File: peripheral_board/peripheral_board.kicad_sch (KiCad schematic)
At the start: 131 parts, among them CN1 DF11-16DP-2DSA(08), J1 Conn_01x06, J2 Conn_ARM_JTAG_SWD_10, J3 Conn_01x03, J4 Conn_01x03, J5 Conn_01x05, SW1 EVPAA602W, SW2 EVPAA602W, SW3 EVPAA602W, U1 RP2040, U2 W5500, U3 AZ1117CH-3.3TRG1, U4 SN74AHC1G125DBVR, U5 KSZ8795CLXIC, U6 W25Q128JVSIQTR, Y1 12MHZ, Y2 25MHZ, Y3 25MHZ

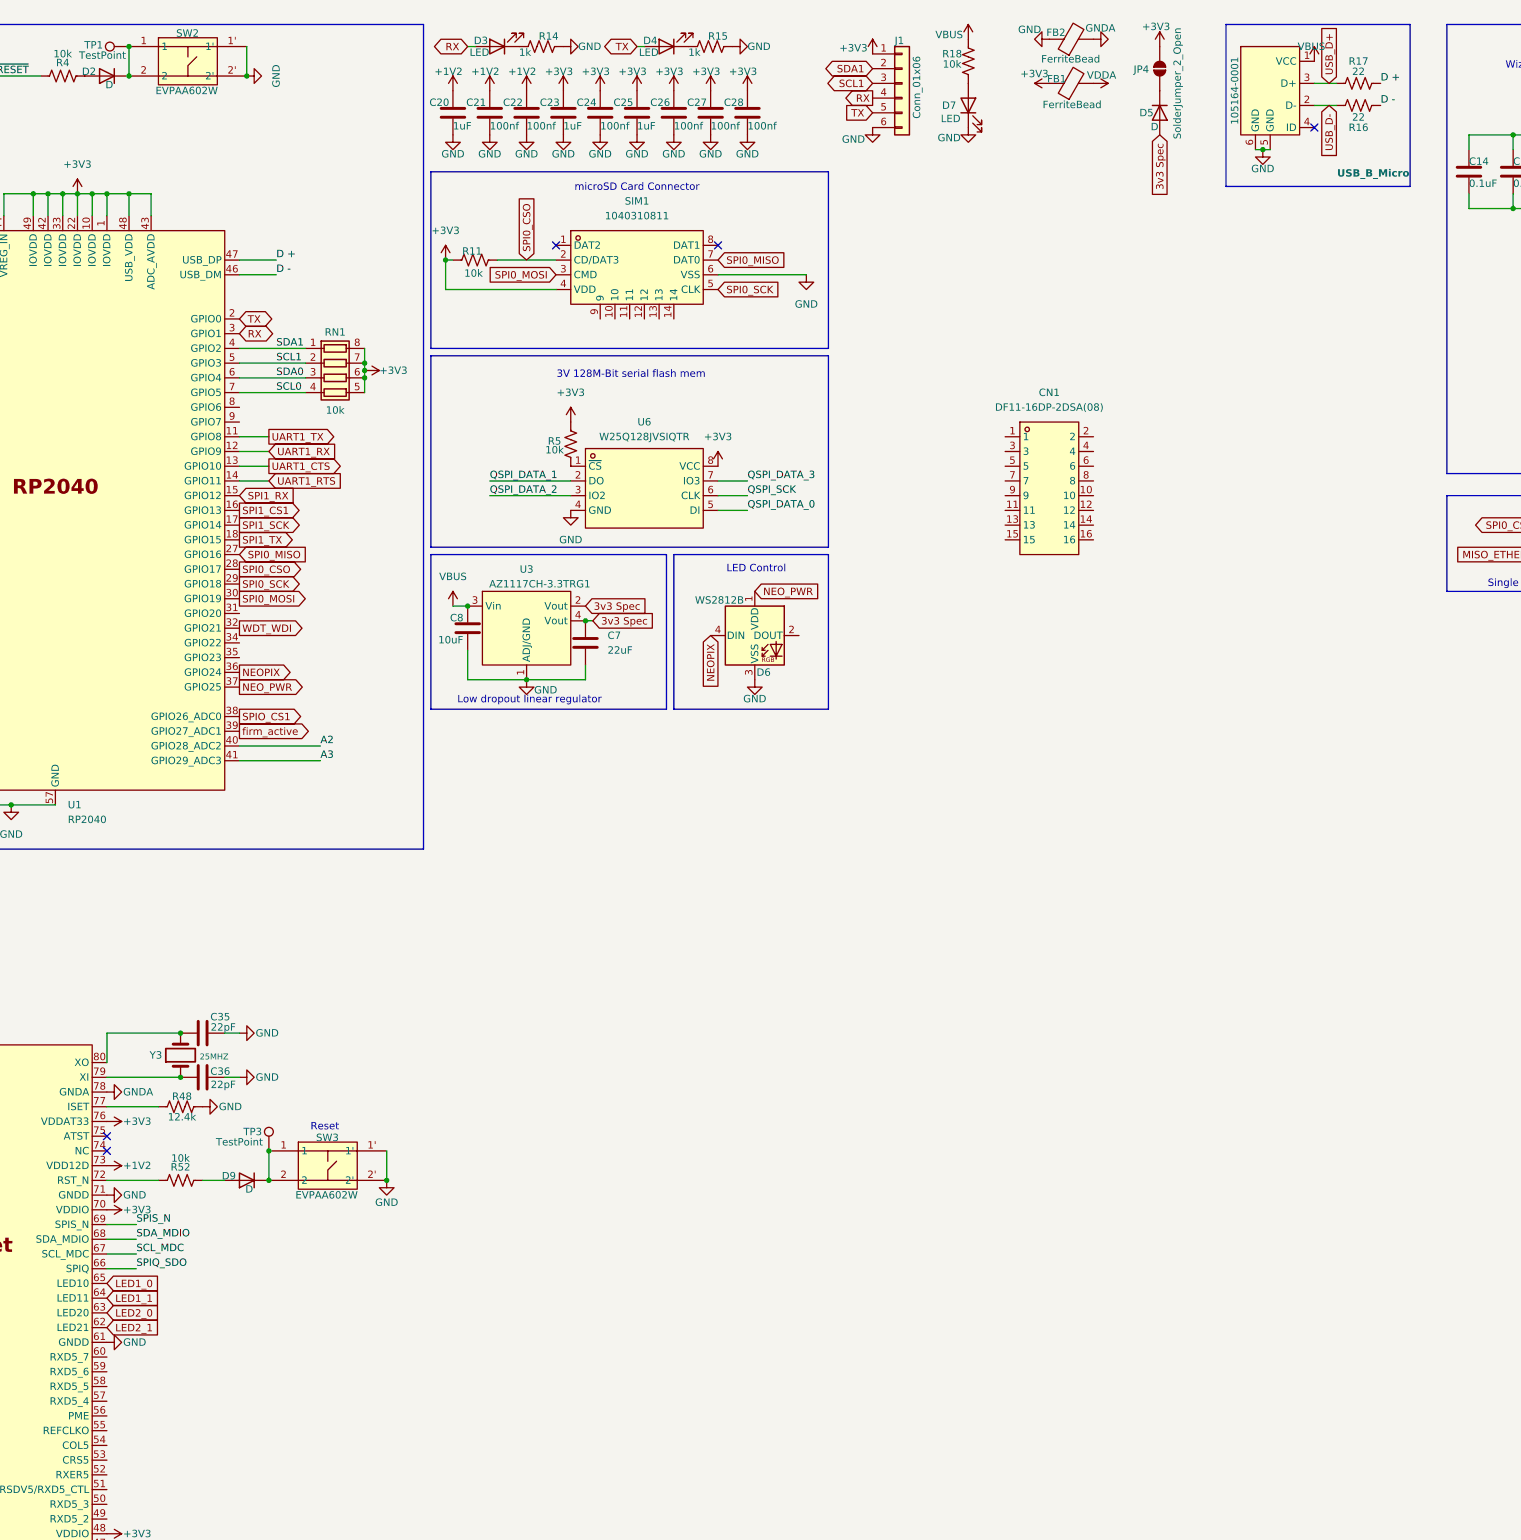
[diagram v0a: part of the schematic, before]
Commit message: Added some labels to the WIP
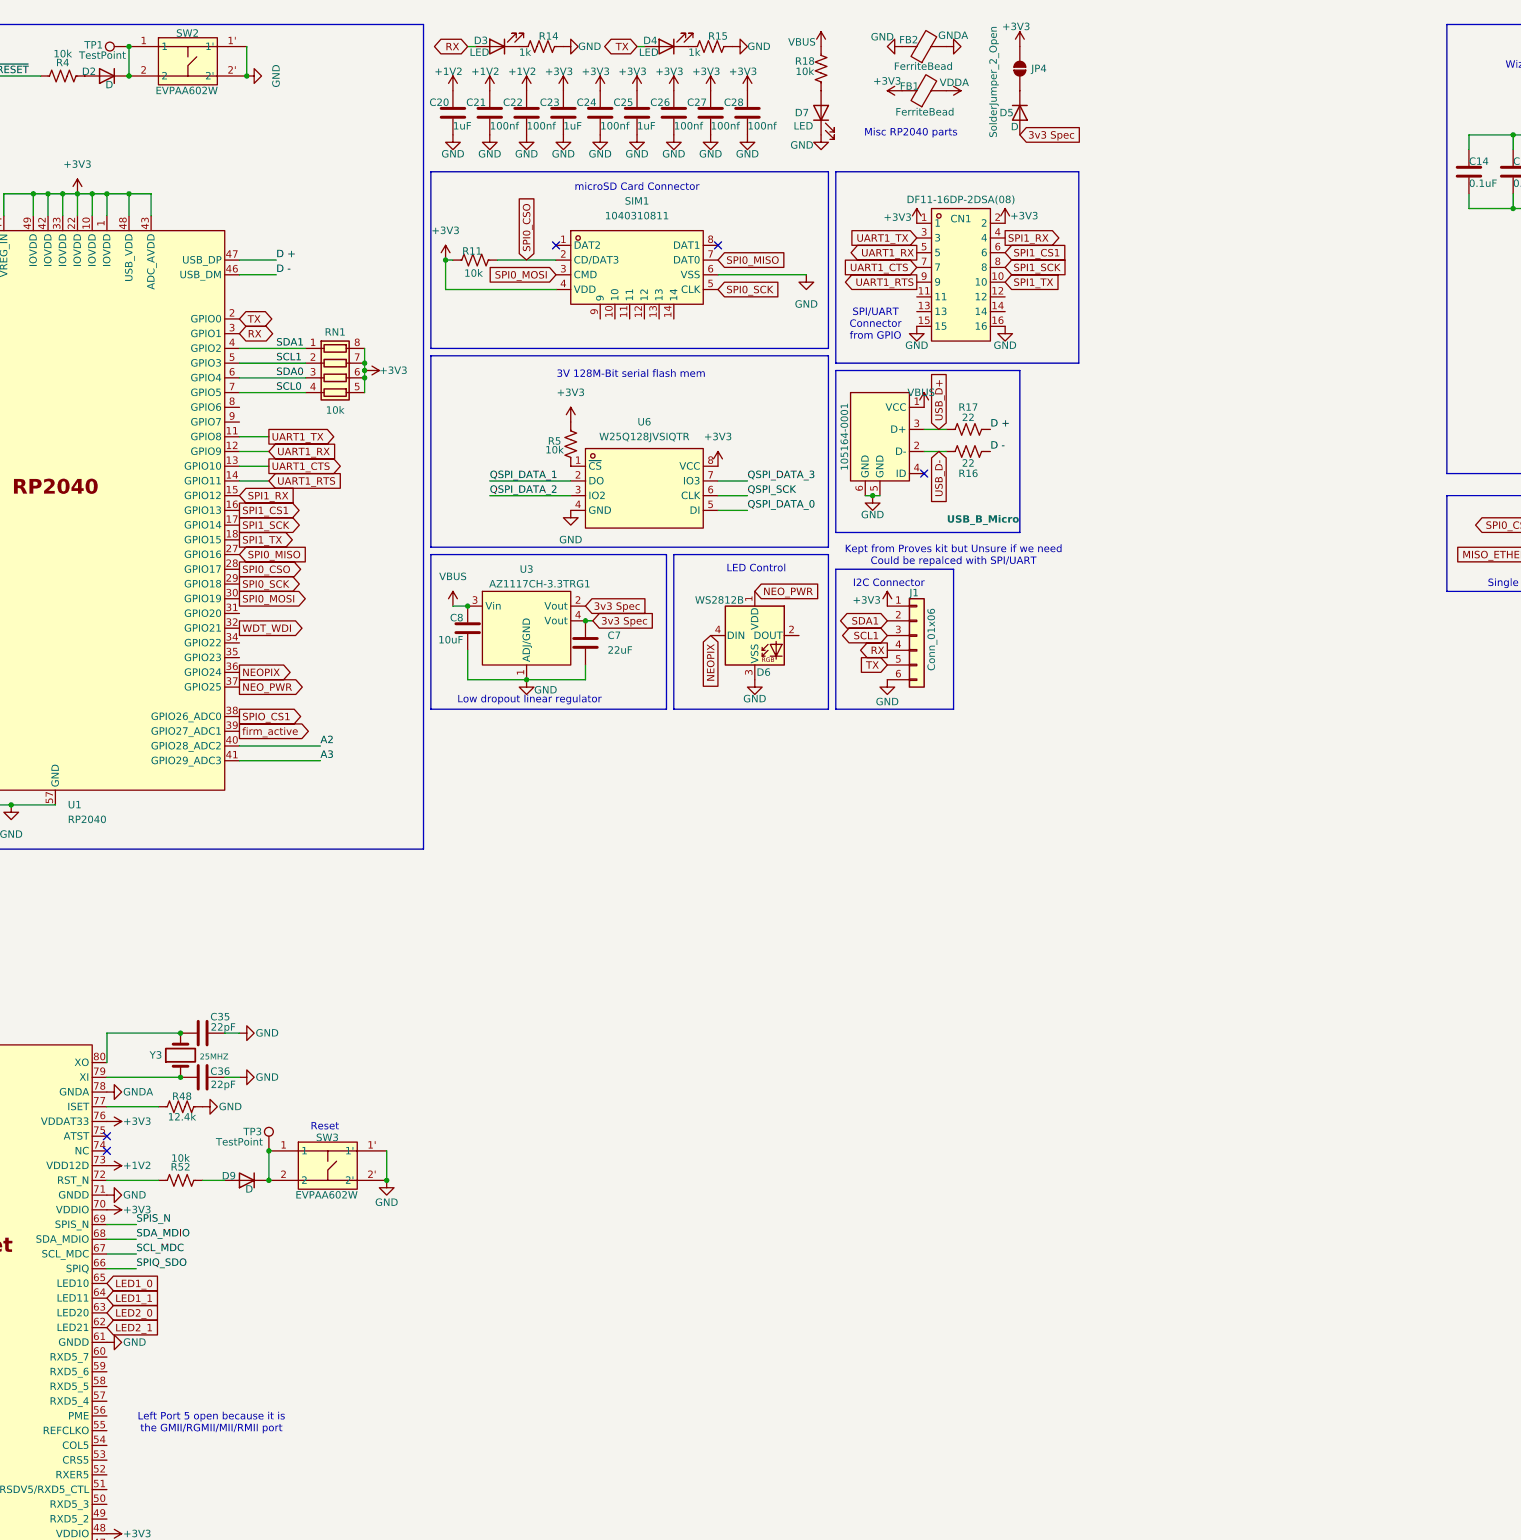
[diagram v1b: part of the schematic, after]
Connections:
- net +3V3: now also CN1.1, CN1.2
- net GND: now also CN1.15, CN1.16
- net SPI1_CS1: now also CN1.6
- net SPI1_RX: now also CN1.4
- net SPI1_SCK: now also CN1.8
- net SPI1_TX: now also CN1.10
- net UART1_CTS: now also CN1.7
- net UART1_RTS: now also CN1.9
- net UART1_RX: now also CN1.5
- net UART1_TX: now also CN1.3
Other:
- note added: "I2C Connector"
- note added: "Kept from Proves kit but Unsure if we need Could be repalced with SPI/UART"
- note added: "Left Port 5 open because it is the GMII/RGMII/MII/RMII port"
- note added: "Misc RP2040 parts"
- note added: "SPI/UART Connector from GPIO"
- moved on the sheet: CN1, D5, D7, FB1, FB2, J1, JP4, R16, R17, R18, USB_B_Micro

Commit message: Add a few changes with some labels
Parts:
- added D10, D11: LED, LED_SMD:LED_0603_1608Metric, symbol Device:LED
- added R53, R55: 330, Resistor_SMD:R_0603_1608Metric, symbol Device:R_US
- added R54, R56: 4.7k, Resistor_SMD:R_0603_1608Metric, symbol Device:R_US
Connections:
- net +3V3: now also R53.2, R54.1, R55.2, R56.1
- net INTR_N: now reaches U5.23 (INTR_N)
- net INTR_N: now also D10.1 (K), R54.2
- net PME_N: now reaches U5.56 (PME)
- net PME_N: now also D11.1 (K), R56.2
- new net: D11.2 (A), R55.1
- new net: D10.2 (A), R53.1
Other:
- note added: "Can remove the 100nf caps"
- note added: "INT"
- note added: "PME"
- company: (none) -> Bronco Space
- title: (none) -> Peripheral Board with Ethernet Switch
- moved on the sheet: C35, C36, D9, R48, R52, SW3, TP3, U4, U5, Y3

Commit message: Added libraries
Added some global libraries to local for ease of use. Added decoupling caps from the dev board.
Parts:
- added C33, C37, C40, C42, C45, C47, C48, C49: 0.1uF, Capacitor_SMD:C_0402_1005Metric, symbol Device:C
- added C34, C39, C41: 100uF, Capacitor_SMD:C_0402_1005Metric, symbol Device:C
- added C38, C43: 0.01uF, Capacitor_SMD:C_0402_1005Metric, symbol Device:C
- added C44, C46: 22uF, Capacitor_SMD:C_0402_1005Metric, symbol Device:C
- added FB3, FB4: FerriteBead, Inductor_SMD:L_0603_1608Metric, symbol Device:FerriteBead
- added JP5, JP6: SolderJumper_2_Open, Jumper:SolderJumper-2_P1.3mm_Open_RoundedPad1.0x1.5mm, symbol Jumper:SolderJumper_2_Open
- added U7: NCP130AMX120TCG, easyeda2kicad:XDFN-6_L1.2-W1.2-P0.40-BL-EP, symbol easyeda2kicad_local:NCP130AMX120TCG
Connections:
- net GND: now also FB2.2, C33.1, C34.1, C37.1, C38.1, C39.1, C40.1, C41.1, C42.1, C43.1, C44.1, C45.1, C46.1, C47.1, C48.1, C49.1, U7.5 (GND), U7.7 (EP); no longer FB2.1
- net GNDA: now also FB2.1; no longer FB2.2
- new net: FB3.2, JP5.2 (B)
- new net: C39.2, C40.2, FB3.1, FB4.1, U7.1 (VOUT)
- new net: FB4.2, JP6.2 (B)
- new net +5V: C33.2, U7.3 (EN), U7.4 (BIAS), U7.6 (VIN)
- new net V1.2A: C34.2, C37.2, C38.2, C44.2, C45.2, JP5.1 (A)
- new net V1.2D: C41.2, C42.2, C43.2, C46.2, C47.2, C48.2, C49.2, JP6.1 (A)
- no-connect marks 22 -> 23
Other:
- note added: "1.2V Digital Current Probe"
- note added: "Decoupling Device Pin 1 VDD12A for analog 1.2V"
- note added: "Decoupling Device Pin 26, 42 & 73 for VDD12D for digital 1.2V"
- note added: "Page 5 of the Ethernet switch data sheet"
- note added: "V1.2A Current Probe"
- moved on the sheet: C35, C36, D10, D11, D9, J3, J4, J5, R48, R49, R50, R51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

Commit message: Slight update
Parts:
- JP1, JP2, JP3, JP4, JP5, JP6: now in the parts list
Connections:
- net SPIO_CS1 is gone; now on net SPI0_CS1: U1.38 (GPIO26_ADC0)
- net +1V2: no longer U5.1 (VDD12A), U5.26 (VDD12D), U5.42 (VDD12D), U5.73 (VDD12D)
- net V1.2A: now also U5.1 (VDD12A)
- net V1.2D: now also U5.26 (VDD12D), U5.42 (VDD12D), U5.73 (VDD12D)
- net A2: no longer names the net of U1.40 (GPIO28_ADC2)
- net A3: no longer names the net of U1.41 (GPIO29_ADC3)
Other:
- note added: "Can remove the 100nf caps According to Andrew"
- note added: "Should this be coupled with ~{RESET}"
- note removed: "Can remove the 100nf caps"
- moved on the sheet: D9, R52, SW3, TP3

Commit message: Created subpages
Added subpages for the schematic
Did a quick overview
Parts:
- removed C1, C19, C2, C3, C35, C36, C4, C5, C9: 22pF, Capacitor_SMD:C_0402_1005Metric, symbol Device:C
- removed C10, C15, C18, C8: 10uF, Capacitor_SMD:C_0402_1005Metric, symbol Device:C
- removed C11, C12, C13, C14, C16, C17, C33, C37, C40, C42, C45, C47, C48, C49: 0.1uF, Capacitor_SMD:C_0402_1005Metric, symbol Device:C
- removed C20, C23, C25: 1uF, Capacitor_SMD:C_0402_1005Metric, symbol Device:C
- removed C21, C22, C24, C26, C27, C28: 100nf, Capacitor_SMD:C_0402_1005Metric, symbol Device:C
- removed C29, C30, C31, C32: 1000pf, Capacitor_SMD:C_0402_1005Metric, symbol Device:C
- removed C34, C39, C41: 100uF, Capacitor_SMD:C_0402_1005Metric, symbol Device:C
- removed C38, C43: 0.01uF, Capacitor_SMD:C_0402_1005Metric, symbol Device:C
- removed C44, C46, C7: 22uF, Capacitor_SMD:C_0402_1005Metric, symbol Device:C
- removed C6: 10nf, Capacitor_SMD:C_0402_1005Metric, symbol Device:C
- removed CN1: DF11-16DP-2DSA(08), easyeda2kicad:CONN-TH_DF11-16DP-2DSA-08, symbol easyeda2kicad:DF11-16DP-2DSA(08)
- removed D1, D2, D5, D9: D, Diode_SMD:D_SOD-323F, symbol Device:D
- removed D10, D11, D3, D4, D7, D8: LED, LED_SMD:LED_0603_1608Metric, symbol Device:LED
- removed D6: WS2812B, LED_SMD:LED_WS2812B_PLCC4_5.0x5.0mm_P3.2mm, symbol LED:WS2812B
- removed FB1, FB2, FB3, FB4: FerriteBead, Inductor_SMD:L_0603_1608Metric, symbol Device:FerriteBead
- removed J1: Conn_01x06, Connector_PinHeader_2.54mm:PinHeader_1x06_P2.54mm_Vertical, symbol Connector_Generic:Conn_01x06
- removed J2: Conn_ARM_JTAG_SWD_10, symbol Connector:Conn_ARM_JTAG_SWD_10
- removed J3, J4: Conn_01x03, Connector_Molex:Molex_KK-396_A-41791-0003_1x03_P3.96mm_Vertical, symbol Connector_Generic:Conn_01x03
- removed J5: Conn_01x05, Connector_PinHeader_1.00mm:PinHeader_1x05_P1.00mm_Vertical, symbol Connector_Generic:Conn_01x05
- removed JP1, JP2, JP3, JP4, JP5, JP6: SolderJumper_2_Open, Jumper:SolderJumper-2_P1.3mm_Open_RoundedPad1.0x1.5mm, symbol Jumper:SolderJumper_2_Open
- removed R1, R11, R18, R19, R2, R3, R4, R49, R5, R50, R51, R52: 10k, Resistor_SMD:R_0603_1608Metric, symbol Device:R_US
- removed R10, R6, R7, R8: 49.9, Resistor_SMD:R_0603_1608Metric, symbol Device:R_US
- removed R12: 1M, Resistor_SMD:R_0603_1608Metric, symbol Device:R_US
- removed R13, R48: 12.4k, Resistor_SMD:R_0603_1608Metric, symbol Device:R_US
- removed R14, R15: 1k, Resistor_SMD:R_0603_1608Metric, symbol Device:R_US
- removed R16, R17: 22, Resistor_SMD:R_0603_1608Metric, symbol Device:R_US
- removed R20, R21, R22, R23, R24, R25, R27, R28, R29, R30, R31, R32, R34, R35, R36, R37, R38, R39, R40, R41, R42, R43, R44, R45: 51, Resistor_SMD:R_0603_1608Metric, symbol Device:R_US
- removed R26, R33, R46, R47: 75, Resistor_SMD:R_0603_1608Metric, symbol Device:R_US
- removed R53, R55: 330, Resistor_SMD:R_0603_1608Metric, symbol Device:R_US
- removed R54, R56: 4.7k, Resistor_SMD:R_0603_1608Metric, symbol Device:R_US
- removed R9: 10, Resistor_SMD:R_0603_1608Metric, symbol Device:R_US
- removed RJ2, RJ3, RJ4, RJ5, RJ6: RJHSE5384, easyeda2kicad:RJ45-TH_RJHSE5384, symbol easyeda2kicad:RJHSE5384
- removed RN1, RN2: 10k, Resistor_SMD:R_Array_Convex_4x0603, symbol Device:R_Pack04
- removed SIM1: 1040310811, easyeda2kicad:SIM-SMD_8P-1040310811, symbol easyeda2kicad:1040310811
- removed SW1, SW2, SW3: EVPAA602W, easyeda2kicad:KEY-TH_4P-L3.5-W4.9-P2.80-LS4.3, symbol easyeda2kicad:EVPAA602W
- removed TP1, TP2, TP3: TestPoint, symbol Connector:TestPoint
- removed U1: RP2040, easyeda2kicad:LQFN-56_L7.0-W7.0-P0.4-EP, symbol easyeda2kicad:RP2040
- removed U2: W5500, easyeda2kicad:LQFP-48_L7.0-W7.0-P0.50-LS9.0-BL, symbol easyeda2kicad:W5500
- removed U3: AZ1117CH-3.3TRG1, easyeda2kicad:SOT-223-3_L6.5-W3.4-P2.30-LS7.0-BR, symbol easyeda2kicad:AZ1117CH-3.3TRG1
- removed U4: SN74AHC1G125DBVR, easyeda2kicad:SOT-23-5_L3.0-W1.7-P0.95-LS2.8-BR, symbol easyeda2kicad:SN74AHC1G125DBVR
- removed U5: KSZ8795CLXIC, easyeda2kicad:LQFP-80_L10.0-W10.0-P0.40-LS12.2-BL, symbol easyeda2kicad:KSZ8795CLXIC
- removed U6: W25Q128JVSIQTR, easyeda2kicad:SOIC-8_L5.3-W5.3-P1.27-LS8.0-BL, symbol easyeda2kicad:W25Q128JVSIQTR
- removed U7: NCP130AMX120TCG, easyeda2kicad:XDFN-6_L1.2-W1.2-P0.40-BL-EP, symbol easyeda2kicad_local:NCP130AMX120TCG
- removed USB_B_Micro: 105164-0001, easyeda2kicad:MICRO-USB-SMD_5P-P0.65-H-F_105164-0001, symbol easyeda2kicad:105164-0001
- removed Y1: 12MHZ, Crystal:Crystal_SMD_2012-2Pin_2.0x1.2mm, symbol Device:Crystal
- removed Y2: 25MHZ, Crystal:Crystal_SMD_3225-4Pin_3.2x2.5mm, symbol Device:Crystal
- removed Y3: 25MHZ, Crystal:Crystal_SMD_2012-2Pin_2.0x1.2mm, symbol Device:Crystal
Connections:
- no-connect marks 23 -> 0
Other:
- added sheet 5-Port_Ethernet_Switch (ethernet_switch.kicad_sch)
- added sheet Raspberry_pi (rp.kicad_sch)
- added sheet Wiznet (Wiznet.kicad_sch)
- note removed: "0 0 0 = 10BT Half-duplex, Auto-negotiation disabled 0 0 1 = 10BT Full-duplex, Auto-negotiation disabled 0 1 0 = 100BT Half-duplex, Auto-negotiation disabled 0 1 1 = 100BT Full-duplex, Auto-negotiation disabled 1 0 0 = 100BT Half-duplex, Auto-negotiation enabled 1 1 1 = All capable, Auto-negotiation enabled (DEFAULT)"
- note removed: "1.2V Digital Current Probe"
- note removed: "3V 128M-Bit serial flash mem"
- note removed: "Arm 10-pin, 0.05" JTAG/SWD connector"
- note removed: "Breakout Pins"
- note removed: "Can remove the 100nf caps According to Andrew"
- note removed: "Decoupling Device Pin 1 VDD12A for analog 1.2V"
- note removed: "Decoupling Device Pin 26, 42 & 73 for VDD12D for digital 1.2V"
- note removed: "Green(9) is Speed WHICH IS LED#_1 Yellow(11) is Link/Act WHICH IS LED#_0"
- note removed: "I2C Connector"
- note removed: "INT"
- note removed: "Kept from Proves kit but Unsure if we need Could be repalced with SPI/UART"
- note removed: "LED Control"
- note removed: "Left Port 5 open because it is the GMII/RGMII/MII/RMII port"
- note removed: "Low dropout linear regulator"
- note removed: "Misc RP2040 parts"
- note removed: "PME"
- note removed: "Page 5 of the Ethernet switch data sheet"
- note removed: "RJ45 Port 1"
- note removed: "RJ45 Port 2"
- note removed: "RJ45 Port 3"
- note removed: "RJ45 Port 4"
- note removed: "RJ45 connector"
- note removed: "Reset"
- note removed: "SPI/UART Connector from GPIO"
- note removed: "Should this be coupled with ~{RESET}"
- note removed: "Single Bus Buffer gate with 3-state output"
- note removed: "V1.2A Current Probe"
- note removed: "Wiznet Ethernet controller"
- note removed: "microSD Card Connector"

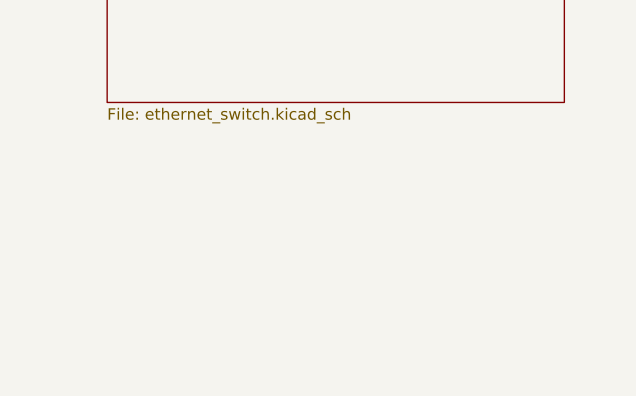
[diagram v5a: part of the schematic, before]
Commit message: Put in the strap in mode
Found a different configuration that should work as the 4 port switch. Added the courtyards to all the parts.
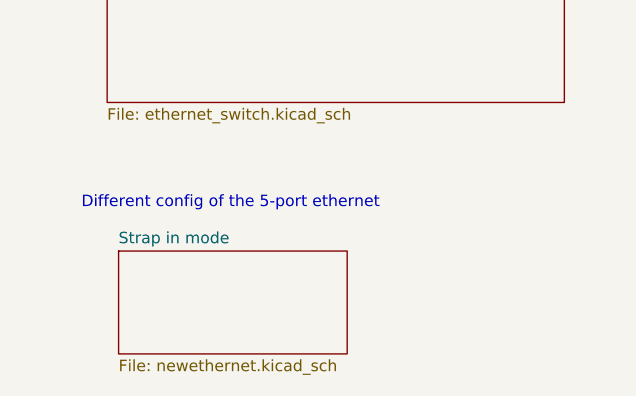
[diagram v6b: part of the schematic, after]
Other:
- added sheet Strap in mode (newethernet.kicad_sch)
- note added: "Different config of the 5-port ethernet"
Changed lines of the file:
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@@
 		(comment 2 "By John Pollak")
+	)
+	(text "Different config of the 5-port ethernet\n"
+		(exclude_from_sim no)
+		(at 39.116 125.476 0)
+		(effects
+			(font
+				(size 1.27 1.27)
+			)
+		)
 	)
 	(sheet
@@
 				)
 			)
+		)
+	)
+	(sheet
+		(at 26.67 130.81)
+		(size 25.4 11.43)
+		(exclude_from_sim yes)
+		(in_bom no)
+		(on_board no)
+		(dnp yes)
+		(fields_autoplaced yes)
+		(stroke
+			(width 0.1524)
+			(type solid)
+		)
+		(fill
+			(color 0 0 0 0.0000)
+		)
+		(property "Sheetname" "Strap in mode"
+			(at 26.67 130.0984 0)
+			(effects
+				(font
+					(size 1.27 1.27)
+				)
+				(justify left bottom)
+			)
+		)
+		(property "Sheetfile" "newethernet.kicad_sch"
+			(at 26.67 142.8246 0)
+			(effects
+				(font
+					(size 1.27 1.27)
+				)
+				(justify left top)
+			)
+		)
+		(instances
+			(project "peripheral_board"
+				(path "/14f8712f-1710-40cb-b01e-cc9b3c4405bd"
+					(page "13")
+				)
+			)
